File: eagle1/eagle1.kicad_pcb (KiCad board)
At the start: 2 copper layers, 600 x 11.4 mm, 2 parts, among them J1 USB-C Plug, J2 USB-C Plug

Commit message: Fix silkscreen; add coverlay notation layer
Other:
- board text added: "COVERLAY"
- board text added: "FOR USE IN TESTING ONLY - DO NOT CONNECT TO HOST - DO NOT CONNECT TO ANYTHING BUT INTENDED PORTS ON TESTER/EUT"
- board text added: "TO EUT 被测设备"
- board text added: "TO TESTER 至测试仪"
- board text removed: "FOR USE IN TESTING ONLY - DO NOT CONNECT TO HOST - DO NOT CONNECT TO ANYTHING BUT INTENDED PORTS ON TESTER/EQUIPMENT UNDER TEST"
- board text removed: "TO SASSERIDES"
- board text removed: "TO TYCHO"
- board text removed: "前往萨塞里德"
- board text removed: "致第谷"
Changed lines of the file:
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@@
   (gr_line (start 605 55.7) (end 625 55.7)
     (stroke (width 0.15) (type default)) (layer "Dwgs.User"))
+  (gr_rect (start 28.5 44.3) (end 621.45 55.7)
+    (stroke (width 0.15) (type default)) (fill none) (layer "Cmts.User"))
   (gr_line (start 625 55.7) (end 615 55.7)
     (stroke (width 0.1) (type default)) (layer "Edge.Cuts"))
@@
   (gr_line (start 45.95 55.7) (end 25 55.7)
     (stroke (width 0.1) (type default)) (layer "Edge.Cuts"))
-  (gr_text "仅供测试使用 - 请勿连接主机 - 请勿连接测试仪/被测设备上的指定端口以外的任何其他端口" (at 469.466664 55.1) (layer "B.SilkS")
+  (gr_text "TO EUT 被测设备" (at 50 48.3) (layer "B.SilkS")
+    (effects (font (size 2 2) (thickness 0.3)) (justify left bottom))
+  )
+  (gr_text "仅供测试使用 - 请勿连接主机 - 请勿连接测试仪/被测设备上的指定端口以外的任何其他端口" (at 554.05 52.5 180) (layer "B.SilkS")
     (effects (font (size 2 2) (thickness 0.3)) (justify right bottom mirror))
   )
-  (gr_text "仅供测试使用 - 请勿连接主机 - 请勿连接测试仪/被测设备上的指定端口以外的任何其他端口" (at 469.466664 48.3) (layer "B.SilkS")
+  (gr_text "仅供测试使用 - 请勿连接主机 - 请勿连接测试仪/被测设备上的指定端口以外的任何其他端口" (at 428.45 48.3) (layer "B.SilkS")
     (effects (font (size 2 2) (thickness 0.3)) (justify right bottom mirror))
   )
-  (gr_text "仅供测试使用 - 请勿连接主机 - 请勿连接测试仪/被测设备上的指定端口以外的任何其他端口" (at 55.016664 55.1) (layer "B.SilkS")
+  (gr_text "仅供测试使用 - 请勿连接主机 - 请勿连接测试仪/被测设备上的指定端口以外的任何其他端口" (at 221.6 52.5 180) (layer "B.SilkS")
     (effects (font (size 2 2) (thickness 0.3)) (justify right bottom mirror))
   )
-  (gr_text "TO TYCHO" (at 621.1 48) (layer "B.SilkS")
-    (effects (font (size 2 2) (thickness 0.3)) (justify left bottom mirror))
-  )
-  (gr_text "FOR USE IN TESTING ONLY - DO NOT CONNECT TO HOST - DO NOT CONNECT TO ANYTHING BUT INTENDED PORTS ON TESTER/EQUIPMENT UNDER TEST" (at 210.366664 48.3) (layer "B.SilkS")
+  (gr_text "FOR USE IN TESTING ONLY - DO NOT CONNECT TO HOST - DO NOT CONNECT TO ANYTHING BUT INTENDED PORTS ON TESTER/EUT" (at 225.9 48.3) (layer "B.SilkS")
     (effects (font (size 2 2) (thickness 0.3)) (justify right bottom mirror))
   )
-  (gr_text "仅供测试使用 - 请勿连接主机 - 请勿连接测试仪/被测设备上的指定端口以外的任何其他端口" (at 55.016664 48.3) (layer "B.SilkS")
+  (gr_text "仅供测试使用 - 请勿连接主机 - 请勿连接测试仪/被测设备上的指定端口以外的任何其他端口" (at 96 48.3) (layer "B.SilkS")
     (effects (font (size 2 2) (thickness 0.3)) (justify right bottom mirror))
   )
-  (gr_text "FOR USE IN TESTING ONLY - DO NOT CONNECT TO HOST - DO NOT CONNECT TO ANYTHING BUT INTENDED PORTS ON TESTER/EQUIPMENT UNDER TEST" (at 210.366664 55.1) (layer "B.SilkS")
+  (gr_text "FOR USE IN TESTING ONLY - DO NOT CONNECT TO HOST - DO NOT CONNECT TO ANYTHING BUT INTENDED PORTS ON TESTER/EUT" (at 424.95 52.5 180) (layer "B.SilkS")
     (effects (font (size 2 2) (thickness 0.3)) (justify right bottom mirror))
   )
-  (gr_text "致第谷" (at 618.25 55) (layer "B.SilkS")
-    (effects (font (size 2 2) (thickness 0.3)) (justify left bottom mirror))
-  )
-  (gr_text "TO SASSERIDES" (at 29.3 47.25) (layer "F.SilkS")
-    (effects (font (size 1.25 1.25) (thickness 0.2)) (justify left bottom))
-  )
-  (gr_text "仅供测试使用 - 请勿连接主机 - 请勿连接测试仪/被测设备上的指定端口以外的任何其他端口" (at 469.45 55.1) (layer "F.SilkS")
+  (gr_text "TO EUT 被测设备" (at 74 52.5 180) (layer "B.SilkS")
     (effects (font (size 2 2) (thickness 0.3)) (justify left bottom))
   )
-  (gr_text "仅供测试使用 - 请勿连接主机 - 请勿连接测试仪/被测设备上的指定端口以外的任何其他端口" (at 55 48.3) (layer "F.SilkS")
+  (gr_text "仅供测试使用 - 请勿连接主机 - 请勿连接测试仪/被测设备上的指定端口以外的任何其他端口" (at 554 52.5 180) (layer "F.SilkS")
     (effects (font (size 2 2) (thickness 0.3)) (justify left bottom))
   )
-  (gr_text "FOR USE IN TESTING ONLY - DO NOT CONNECT TO HOST - DO NOT CONNECT TO ANYTHING BUT INTENDED PORTS ON TESTER/EQUIPMENT UNDER TEST" (at 210.35 55.1) (layer "F.SilkS")
+  (gr_text "仅供测试使用 - 请勿连接主机 - 请勿连接测试仪/被测设备上的指定端口以外的任何其他端口" (at 96 48.3) (layer "F.SilkS")
     (effects (font (size 2 2) (thickness 0.3)) (justify left bottom))
   )
-  (gr_text "前往萨塞里德" (at 29.1 53.6) (layer "F.SilkS")
-    (effects (font (size 1.75 1.75) (thickness 0.25)) (justify left bottom))
-  )
-  (gr_text "仅供测试使用 - 请勿连接主机 - 请勿连接测试仪/被测设备上的指定端口以外的任何其他端口" (at 469.45 48.3) (layer "F.SilkS")
+  (gr_text "TO TESTER 至测试仪" (at 570.75 48.3) (layer "F.SilkS")
     (effects (font (size 2 2) (thickness 0.3)) (justify left bottom))
   )
-  (gr_text "FOR USE IN TESTING ONLY - DO NOT CONNECT TO HOST - DO NOT CONNECT TO ANYTHING BUT INTENDED PORTS ON TESTER/EQUIPMENT UNDER TEST" (at 210.35 48.3) (layer "F.SilkS")
+  (gr_text "FOR USE IN TESTING ONLY - DO NOT CONNECT TO HOST - DO NOT CONNECT TO ANYTHING BUT INTENDED PORTS ON TESTER/EUT" (at 425.05 52.5 180) (layer "F.SilkS")
     (effects (font (size 2 2) (thickness 0.3)) (justify left bottom))
   )
-  (gr_text "仅供测试使用 - 请勿连接主机 - 请勿连接测试仪/被测设备上的指定端口以外的任何其他端口" (at 55 55.1) (layer "F.SilkS")
+  (gr_text "仅供测试使用 - 请勿连接主机 - 请勿连接测试仪/被测设备上的指定端口以外的任何其他端口" (at 428.45 48.3) (layer "F.SilkS")
+    (effects (font (size 2 2) (thickness 0.3)) (justify left bottom))
+  )
+  (gr_text "TO TESTER 至测试仪" (at 600 52.5 180) (layer "F.SilkS")
+    (effects (font (size 2 2) (thickness 0.3)) (justify left bottom))
+  )
+  (gr_text "FOR USE IN TESTING ONLY - DO NOT CONNECT TO HOST - DO NOT CONNECT TO ANYTHING BUT INTENDED PORTS ON TESTER/EUT" (at 225.9 48.3) (layer "F.SilkS")
+    (effects (font (size 2 2) (thickness 0.3)) (justify left bottom))
+  )
+  (gr_text "仅供测试使用 - 请勿连接主机 - 请勿连接测试仪/被测设备上的指定端口以外的任何其他端口" (at 221.6 52.5 180) (layer "F.SilkS")
     (effects (font (size 2 2) (thickness 0.3)) (justify left bottom))
   )
@@
   )
   (gr_text "FR4 stiffener to be used\nPCB ends." (at 605.55 36.95) (layer "Dwgs.User")
+    (effects (font (size 1 1) (thickness 0.15)) (justify left bottom))
+  )
+  (gr_text "COVERLAY" (at 320.55 42.5) (layer "Cmts.User")
     (effects (font (size 1 1) (thickness 0.15)) (justify left bottom))
   )
@@
     (style (thickness 0.15) (arrow_length 1.27) (text_position_mode 2) (extension_height 0.58642) (extension_offset 0.5) keep_text_aligned)
   )
+  (dimension (type aligned) (layer "Cmts.User")
+    (pts (xy 309.85 55.7) (xy 309.85 44.3))
+    (height -0.55)
+    (gr_text "11.4000 mm" (at 308.15 50 90) (layer "Cmts.User")
+      (effects (font (size 1 1) (thickness 0.15)))
+    )
+    (format (prefix "") (suffix "") (units 3) (units_format 1) (precision 4))
+    (style (thickness 0.15) (arrow_length 1.27) (text_position_mode 0) (extension_height 0.58642) (extension_offset 0.5) keep_text_aligned)
+  )
+  (dimension (type aligned) (layer "Cmts.User")
+    (pts (xy 28.5 44.3) (xy 621.45 44.3))
+    (height -5.4)
+    (gr_text "592.9500 mm" (at 324.975 37.75) (layer "Cmts.User")
+      (effects (font (size 1 1) (thickness 0.15)))
+    )
+    (format (prefix "") (suffix "") (units 3) (units_format 1) (precision 4))
+    (style (thickness 0.15) (arrow_length 1.27) (text_position_mode 0) (extension_height 0.58642) (extension_offset 0.5) keep_text_aligned)
+  )
   (via (at 31.15 54.3) (size 0.8) (drill 0.4) (layers "F.Cu" "B.Cu") (free) (net 11))

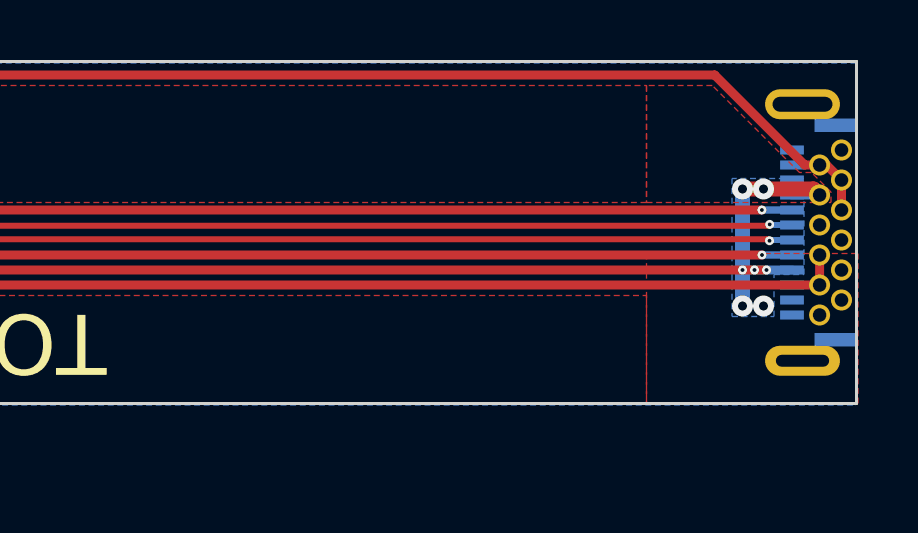
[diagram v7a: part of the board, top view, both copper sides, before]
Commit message: Add to silkscreen
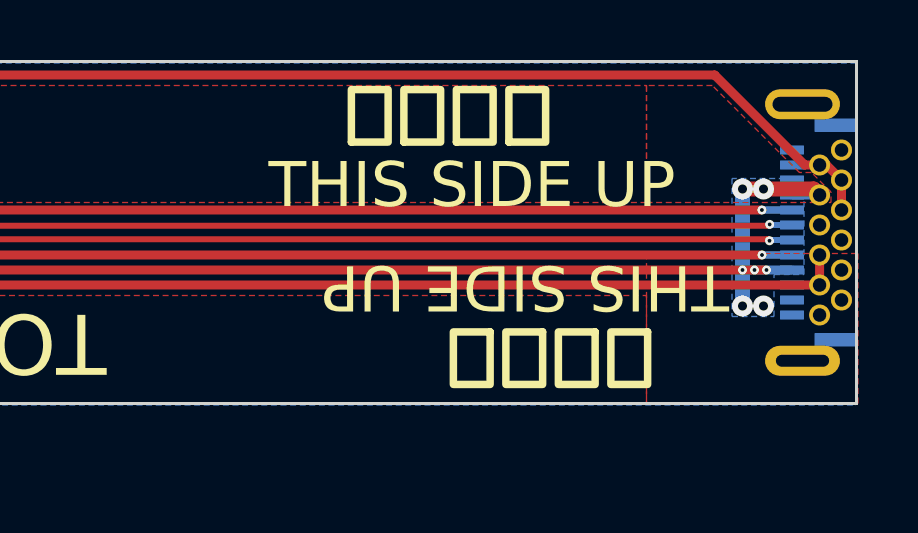
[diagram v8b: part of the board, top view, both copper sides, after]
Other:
- board text added: "THIS SIDE UP"
- board text added: "这边朝上"
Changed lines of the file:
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@@
   (gr_line (start 45.95 55.7) (end 25 55.7)
     (stroke (width 0.1) (type default)) (layer "Edge.Cuts"))
-  (gr_text "TO EUT 被测设备" (at 50 48.3) (layer "B.SilkS")
-    (effects (font (size 2 2) (thickness 0.3)) (justify left bottom))
+  (gr_text "THIS SIDE UP" (at 44.5 49.2) (layer "B.SilkS")
+    (effects (font (size 1.5 1.5) (thickness 0.22)) (justify left bottom mirror))
+  )
+  (gr_text "TO EUT 被测设备" (at 74 48.3) (layer "B.SilkS")
+    (effects (font (size 2 2) (thickness 0.3)) (justify left bottom mirror))
   )
   (gr_text "仅供测试使用 - 请勿连接主机 - 请勿连接测试仪/被测设备上的指定端口以外的任何其他端口" (at 554.05 52.5 180) (layer "B.SilkS")
@@
     (effects (font (size 2 2) (thickness 0.3)) (justify right bottom mirror))
   )
+  (gr_text "THIS SIDE UP" (at 29.25 51.2 180) (layer "B.SilkS")
+    (effects (font (size 1.5 1.5) (thickness 0.22)) (justify left bottom mirror))
+  )
   (gr_text "FOR USE IN TESTING ONLY - DO NOT CONNECT TO HOST - DO NOT CONNECT TO ANYTHING BUT INTENDED PORTS ON TESTER/EUT" (at 225.9 48.3) (layer "B.SilkS")
     (effects (font (size 2 2) (thickness 0.3)) (justify right bottom mirror))
@@
     (effects (font (size 2 2) (thickness 0.3)) (justify right bottom mirror))
   )
-  (gr_text "TO EUT 被测设备" (at 74 52.5 180) (layer "B.SilkS")
-    (effects (font (size 2 2) (thickness 0.3)) (justify left bottom))
+  (gr_text "这边朝上" (at 31.7 53.2 180) (layer "B.SilkS")
+    (effects (font (size 1.75 1.75) (thickness 0.25)) (justify left bottom mirror))
+  )
+  (gr_text "TO EUT 被测设备" (at 50 52.5 180) (layer "B.SilkS")
+    (effects (font (size 2 2) (thickness 0.3)) (justify left bottom mirror))
+  )
+  (gr_text "这边朝上" (at 42 47.05) (layer "B.SilkS")
+    (effects (font (size 1.75 1.75) (thickness 0.25)) (justify left bottom mirror))
+  )
+  (gr_text "THIS SIDE UP" (at 605.4 49.3) (layer "F.SilkS")
+    (effects (font (size 1.5 1.5) (thickness 0.22)) (justify left bottom))
   )
   (gr_text "仅供测试使用 - 请勿连接主机 - 请勿连接测试仪/被测设备上的指定端口以外的任何其他端口" (at 554 52.5 180) (layer "F.SilkS")
     (effects (font (size 2 2) (thickness 0.3)) (justify left bottom))
   )
+  (gr_text "这边朝上" (at 618.3 53.1 180) (layer "F.SilkS")
+    (effects (font (size 1.75 1.75) (thickness 0.25)) (justify left bottom))
+  )
   (gr_text "仅供测试使用 - 请勿连接主机 - 请勿连接测试仪/被测设备上的指定端口以外的任何其他端口" (at 96 48.3) (layer "F.SilkS")
     (effects (font (size 2 2) (thickness 0.3)) (justify left bottom))
@@
   (gr_text "仅供测试使用 - 请勿连接主机 - 请勿连接测试仪/被测设备上的指定端口以外的任何其他端口" (at 428.45 48.3) (layer "F.SilkS")
     (effects (font (size 2 2) (thickness 0.3)) (justify left bottom))
+  )
+  (gr_text "这边朝上" (at 607.9 47.2) (layer "F.SilkS")
+    (effects (font (size 1.75 1.75) (thickness 0.25)) (justify left bottom))
+  )
+  (gr_text "THIS SIDE UP" (at 620.75 50.95 180) (layer "F.SilkS")
+    (effects (font (size 1.5 1.5) (thickness 0.22)) (justify left bottom))
   )
   (gr_text "TO TESTER 至测试仪" (at 600 52.5 180) (layer "F.SilkS")
@@
         (xy 32 47.95)
         (xy 32 47.85)
-        (xy 32 47.85)
         (xy 32 47.7)
